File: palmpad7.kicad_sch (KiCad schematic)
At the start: 21 parts, among them SW1 SW_Push, SW10 RotaryEncoder_Switch, SW2 SW_Push, SW3 SW_Push, SW4 SW_Push, SW5 SW_Push, SW6 SW_Push, SW7 SW_Push, SW8 RotaryEncoder_Switch, SW9 RotaryEncoder_Switch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

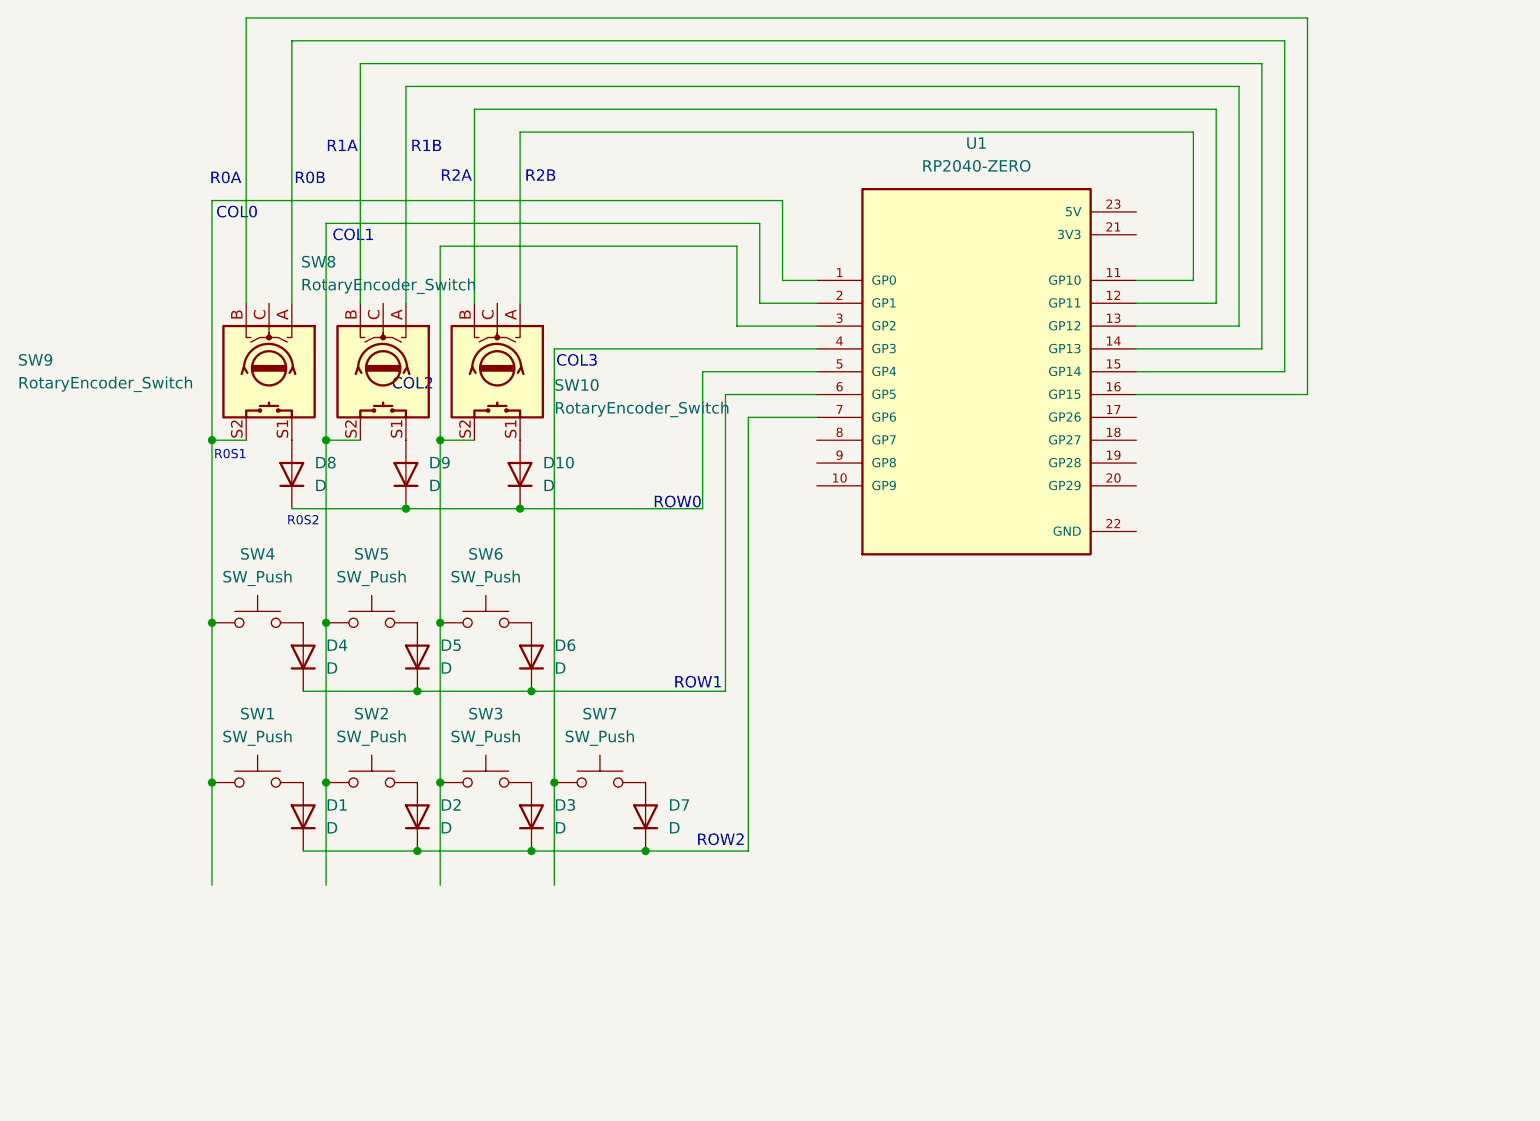
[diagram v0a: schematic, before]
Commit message: Use labels and add OLEDs on schematic
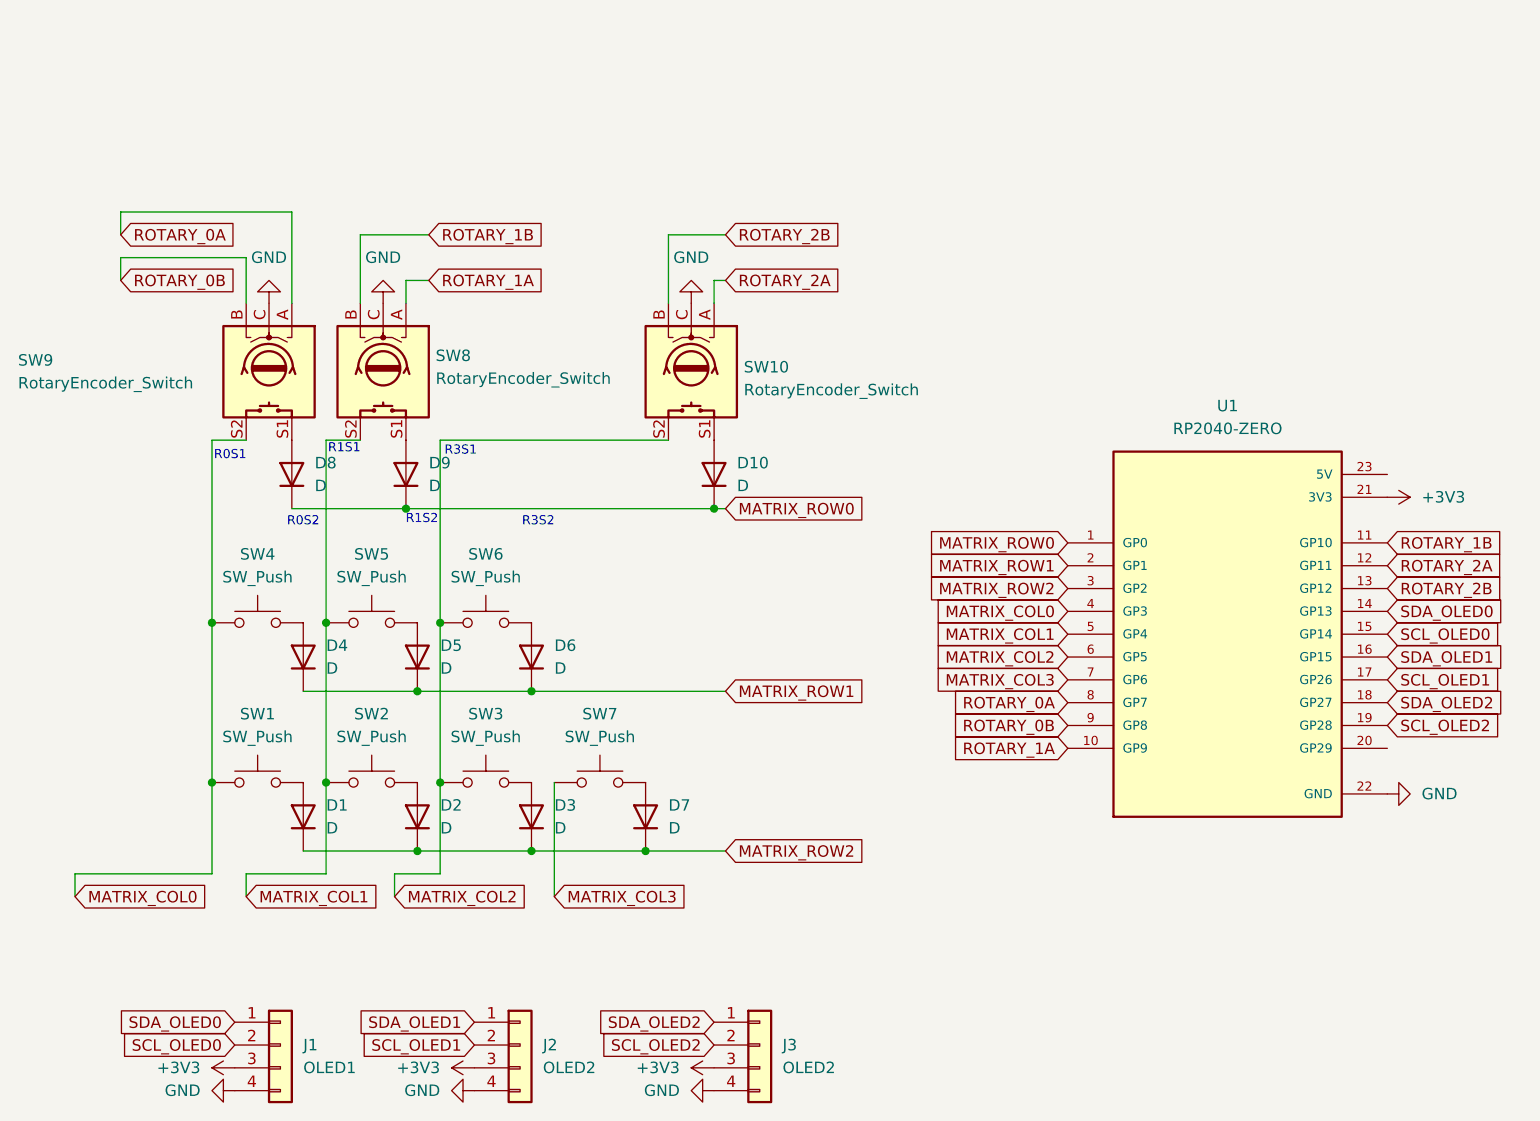
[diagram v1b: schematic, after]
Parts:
- added J1: OLED1, symbol Connector_Generic:Conn_01x04
- added J2, J3: OLED2, symbol Connector_Generic:Conn_01x04
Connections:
- net MATRIX_ROW2: now reaches D1.1 (K), D2.1 (K), D3.1 (K), D7.1 (K)
- net MATRIX_ROW2: now also U1.3 (GP2); no longer U1.7 (GP6)
- net ROTARY_1A: now reaches SW8.A
- net ROTARY_1A: now also U1.10 (GP9); no longer U1.13 (GP12)
- net ROTARY_1B: now reaches SW8.B
- net ROTARY_1B: now also U1.11 (GP10); no longer U1.14 (GP13)
- net GND: now reaches SW8.C
- net GND: now also SW10.C, SW9.C, U1.22 (GND), J1.4 (Pin_4), J2.4 (Pin_4), J3.4 (Pin_4)
- net MATRIX_COL1: now reaches SW2.1, SW5.1, SW8.S2
- net MATRIX_COL1: now also U1.5 (GP4); no longer U1.2 (GP1)
- net MATRIX_ROW1: now reaches D4.1 (K), D5.1 (K), D6.1 (K)
- net MATRIX_ROW1: now also U1.2 (GP1); no longer U1.6 (GP5)
- net MATRIX_COL0: now reaches U1.4 (GP3)
- net MATRIX_COL0: now also SW1.1, SW4.1, SW9.S2; no longer SW7.1
- net ROTARY_0A: now reaches SW9.A
- net ROTARY_0A: now also U1.8 (GP7); no longer U1.15 (GP14)
- net ROTARY_0B: now reaches SW9.B
- net ROTARY_0B: now also U1.9 (GP8); no longer U1.16 (GP15)
- net MATRIX_ROW0: now reaches D10.1 (K), D8.1 (K), D9.1 (K)
- net MATRIX_ROW0: now also U1.1 (GP0); no longer U1.5 (GP4)
- net MATRIX_COL2: now reaches SW10.S2, SW3.1, SW6.1
- net MATRIX_COL2: now also U1.6 (GP5); no longer U1.3 (GP2)
- net ROTARY_2A: now reaches SW10.A
- net ROTARY_2A: now also U1.12 (GP11); no longer U1.11 (GP10)
- net ROTARY_2B: now reaches SW10.B
- net ROTARY_2B: now also U1.13 (GP12); no longer U1.12 (GP11)
- net SCL_OLED1: now reaches U1.17 (GP26)
- net SCL_OLED1: now also J2.2 (Pin_2)
- net SDA_OLED2: now reaches U1.18 (GP27)
- net SDA_OLED2: now also J3.1 (Pin_1)
- net SCL_OLED2: now reaches U1.19 (GP28)
- net SCL_OLED2: now also J3.2 (Pin_2)
- net +3V3: now reaches U1.21 (3V3)
- net +3V3: now also J1.3 (Pin_3), J2.3 (Pin_3), J3.3 (Pin_3)
- new net MATRIX_COL3: SW7.1, U1.7 (GP6)
- new net SCL_OLED0: J1.2 (Pin_2), U1.15 (GP14)
- new net SDA_OLED0: J1.1 (Pin_1), U1.14 (GP13)
- new net SDA_OLED1: J2.1 (Pin_1), U1.16 (GP15)
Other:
- note added: "R1S2"
- note added: "R3S1"
- note added: "R3S2"
- note removed: "COL0"
- note removed: "COL1"
- note removed: "COL2"
- note removed: "COL3"
- note removed: "R0A"
- note removed: "R0B"
- note removed: "R1A"
- note removed: "R1B"
- note removed: "R2A"
- note removed: "R2B"
- note removed: "ROW0"
- note removed: "ROW1"
- note removed: "ROW2"
- moved on the sheet: D10, SW10, U1

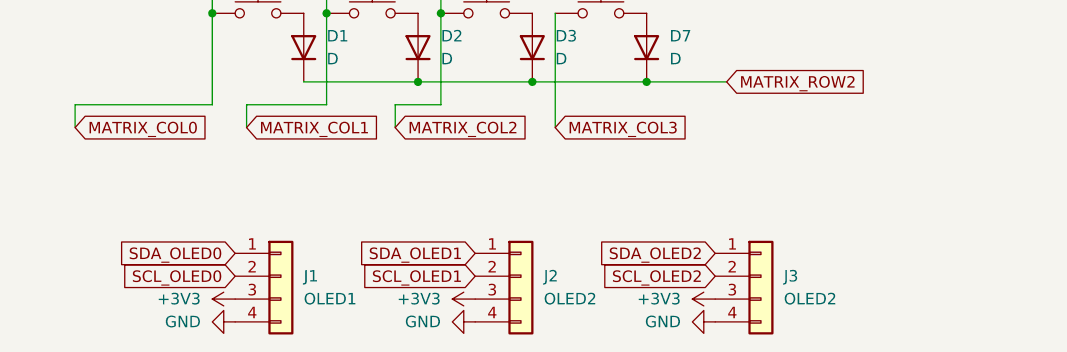
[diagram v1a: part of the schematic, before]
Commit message: Fix OLED pins
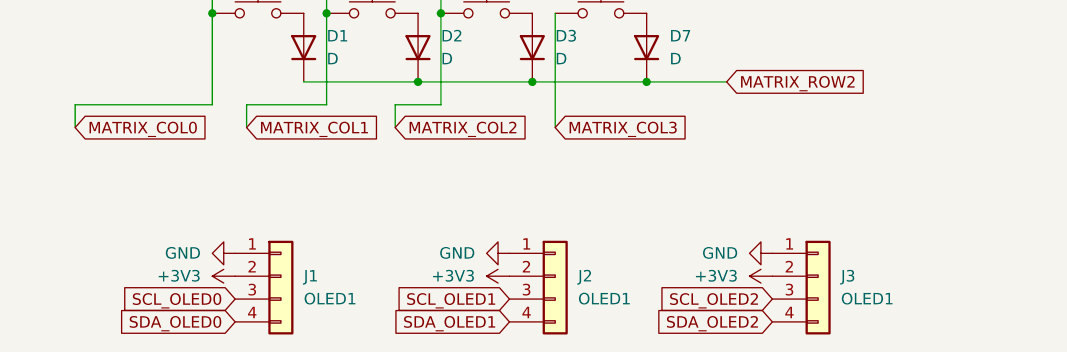
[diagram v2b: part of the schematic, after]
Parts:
- J2, J3: value OLED2 -> OLED1
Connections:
- net +3V3: now also J1.2 (Pin_2), J2.2 (Pin_2), J3.2 (Pin_2); no longer J1.3 (Pin_3), J2.3 (Pin_3), J3.3 (Pin_3)
- net GND: now also J1.1 (Pin_1), J2.1 (Pin_1), J3.1 (Pin_1); no longer J1.4 (Pin_4), J2.4 (Pin_4), J3.4 (Pin_4)
- net SCL_OLED0: now also J1.3 (Pin_3); no longer J1.2 (Pin_2)
- net SCL_OLED1: now also J2.3 (Pin_3); no longer J2.2 (Pin_2)
- net SCL_OLED2: now also J3.3 (Pin_3); no longer J3.2 (Pin_2)
- net SDA_OLED0: now also J1.4 (Pin_4); no longer J1.1 (Pin_1)
- net SDA_OLED1: now also J2.4 (Pin_4); no longer J2.1 (Pin_1)
- net SDA_OLED2: now also J3.4 (Pin_4); no longer J3.1 (Pin_1)

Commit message: start pcb
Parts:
- D1, D10, D2, D3, D4, D5, D6, D7, D8, D9: footprint (none) -> Diode_THT:D_DO-35_SOD27_P7.62mm_Horizontal
- J1, J2, J3: footprint (none) -> Connector_PinSocket_2.54mm:PinSocket_1x04_P2.54mm_Vertical
- SW1, SW2, SW3, SW4, SW5, SW6, SW7: footprint (none) -> Button_Switch_Keyboard:SW_Cherry_MX_1.00u_PCB
- SW10, SW8, SW9: footprint (none) -> Rotary_Encoder:RotaryEncoder_Alps_EC11E-Switch_Vertical_H20mm
- U1: footprint RP2040-ZERO:MODULE_RP2040-ZERO -> RP2040:MODULE_RP2040-ZERO
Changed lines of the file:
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@@
 			)
 		)
-		(property "Footprint" ""
+		(property "Footprint" "Diode_THT:D_DO-35_SOD27_P7.62mm_Horizontal"
 			(at 175.26 123.19 0)
 			(effects
@@
 			)
 		)
-		(property "Footprint" ""
+		(property "Footprint" "Rotary_Encoder:RotaryEncoder_Alps_EC11E-Switch_Vertical_H20mm"
 			(at 150.114 69.85 0)
 			(effects
@@
 			)
 		)
-		(property "Footprint" ""
+		(property "Footprint" "Diode_THT:D_DO-35_SOD27_P7.62mm_Horizontal"
 			(at 162.56 105.41 0)
 			(effects
@@
 			)
 		)
-		(property "Footprint" ""
+		(property "Footprint" "Button_Switch_Keyboard:SW_Cherry_MX_1.00u_PCB"
 			(at 170.18 114.3 0)
 			(effects
@@
 			)
 		)
-		(property "Footprint" ""
+		(property "Footprint" "Rotary_Encoder:RotaryEncoder_Alps_EC11E-Switch_Vertical_H20mm"
 			(at 137.414 69.85 0)
 			(effects
@@
 			)
 		)
-		(property "Footprint" ""
+		(property "Footprint" "Diode_THT:D_DO-35_SOD27_P7.62mm_Horizontal"
 			(at 148.59 85.09 0)
 			(effects
@@
 			)
 		)
-		(property "Footprint" ""
+		(property "Footprint" "Button_Switch_Keyboard:SW_Cherry_MX_1.00u_PCB"
 			(at 132.08 96.52 0)
 			(effects
@@
 		(dnp no)
 		(fields_autoplaced yes)
-		(property "Reference" "#PWR?"
+		(property "Reference" "#PWR0101"
 			(at 146.05 59.69 0)
 			(effects
@@
 			(project ""
 				(path "/5199830b-a9f9-4c8d-9477-d4863d1aab8c"
-					(reference "#PWR?")
+					(reference "#PWR0101")
 					(unit 1)
 				)
@@
 			)
 		)
-		(property "Footprint" ""
+		(property "Footprint" "Button_Switch_Keyboard:SW_Cherry_MX_1.00u_PCB"
 			(at 144.78 96.52 0)
 			(effects
@@
 			)
 		)
-		(property "Footprint" ""
+		(property "Footprint" "Diode_THT:D_DO-35_SOD27_P7.62mm_Horizontal"
 			(at 137.16 105.41 0)
 			(effects
@@
 			)
 		)
-		(property "Footprint" ""
+		(property "Footprint" "Connector_PinSocket_2.54mm:PinSocket_1x04_P2.54mm_Vertical"
 			(at 194.31 148.59 0)
 			(effects
@@
 			)
 		)
-		(property "Footprint" ""
+		(property "Footprint" "Button_Switch_Keyboard:SW_Cherry_MX_1.00u_PCB"
 			(at 132.08 114.3 0)
 			(effects
@@
 			)
 		)
-		(property "Footprint" ""
+		(property "Footprint" "Connector_PinSocket_2.54mm:PinSocket_1x04_P2.54mm_Vertical"
 			(at 165.1 148.59 0)
 			(effects
@@
 			)
 		)
-		(property "Footprint" ""
+		(property "Footprint" "Diode_THT:D_DO-35_SOD27_P7.62mm_Horizontal"
 			(at 182.88 85.09 0)
 			(effects
@@
 			)
 		)
-		(property "Footprint" ""
+		(property "Footprint" "Button_Switch_Keyboard:SW_Cherry_MX_1.00u_PCB"
 			(at 157.48 114.3 0)
 			(effects
@@
 			)
 		)
-		(property "Footprint" ""
+		(property "Footprint" "Connector_PinSocket_2.54mm:PinSocket_1x04_P2.54mm_Vertical"
 			(at 134.62 148.59 0)
 			(effects
@@
 			)
 		)
-		(property "Footprint" ""
+		(property "Footprint" "Diode_THT:D_DO-35_SOD27_P7.62mm_Horizontal"
 			(at 162.56 123.19 0)
 			(effects
@@
 			)
 		)
-		(property "Footprint" ""
+		(property "Footprint" "Diode_THT:D_DO-35_SOD27_P7.62mm_Horizontal"
 			(at 135.89 85.09 0)
 			(effects
@@
 			)
 		)
-		(property "Footprint" ""
+		(property "Footprint" "Button_Switch_Keyboard:SW_Cherry_MX_1.00u_PCB"
 			(at 144.78 114.3 0)
 			(effects
@@
 			)
 		)
-		(property "Footprint" ""
+		(property "Footprint" "Diode_THT:D_DO-35_SOD27_P7.62mm_Horizontal"
 			(at 137.16 123.19 0)
 			(effects
@@
 			)
 		)
-		(property "Footprint" ""
+		(property "Footprint" "Rotary_Encoder:RotaryEncoder_Alps_EC11E-Switch_Vertical_H20mm"
 			(at 184.404 69.85 0)
 			(effects
@@
 			)
 		)
-		(property "Footprint" "RP2040-ZERO:MODULE_RP2040-ZERO"
+		(property "Footprint" "RP2040:MODULE_RP2040-ZERO"
 			(at 240.03 102.87 0)
 			(effects
@@
 			)
 		)
-		(property "Footprint" ""
+		(property "Footprint" "Diode_THT:D_DO-35_SOD27_P7.62mm_Horizontal"
 			(at 149.86 123.19 0)
 			(effects
@@
 			)
 		)
-		(property "Footprint" ""
+		(property "Footprint" "Button_Switch_Keyboard:SW_Cherry_MX_1.00u_PCB"
 			(at 157.48 96.52 0)
 			(effects
@@
 			)
 		)
-		(property "Footprint" ""
+		(property "Footprint" "Diode_THT:D_DO-35_SOD27_P7.62mm_Horizontal"
 			(at 149.86 105.41 0)
 			(effects
